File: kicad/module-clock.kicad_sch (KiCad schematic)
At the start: 9 parts, among them U1 NE555P

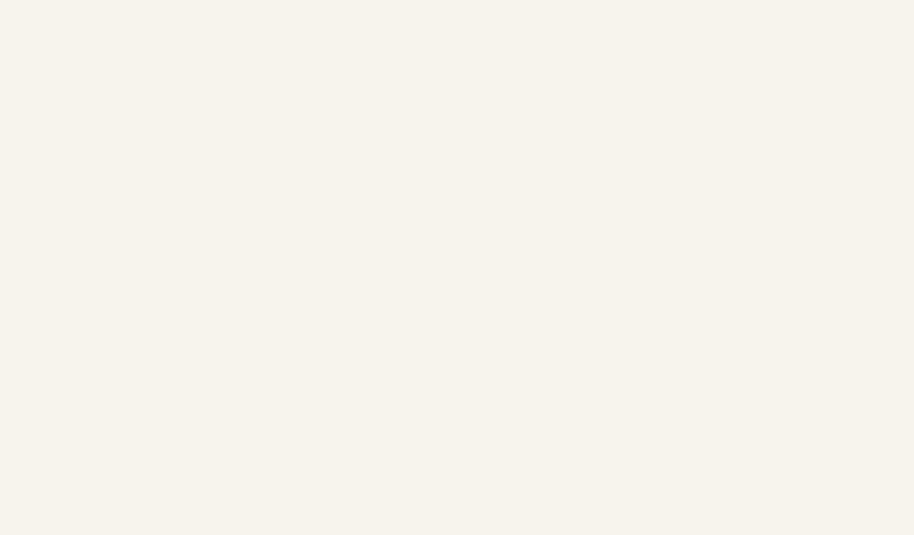
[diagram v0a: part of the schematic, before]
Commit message: Initial monostable mode implementation
Implement a monostable mode using the ne555 chip as a debouncer for the switch
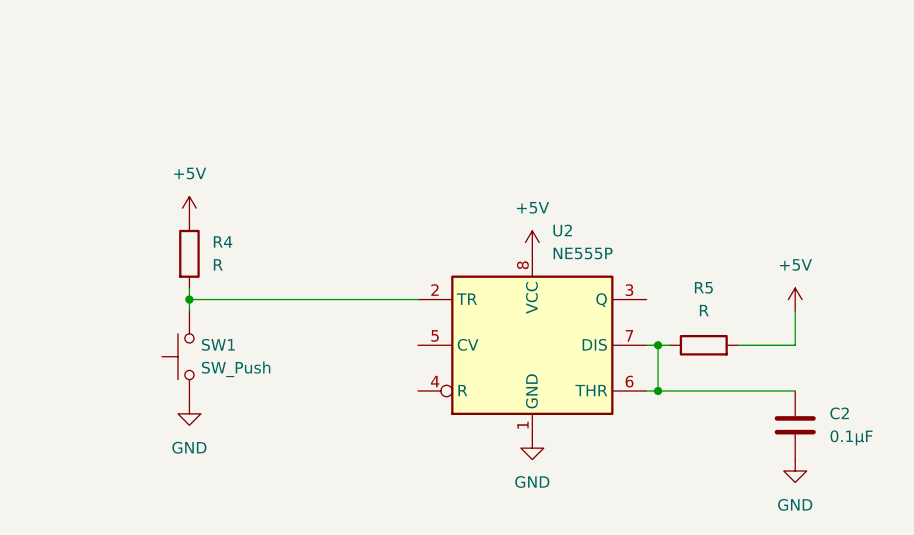
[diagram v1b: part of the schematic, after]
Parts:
- added C2: 0.1μF, symbol Device:C
- added R4, R5: R, symbol Device:R
- added SW1: SW_Push, symbol Switch:SW_Push
- added U2: NE555P, Package_DIP:DIP-8_W7.62mm, symbol Timer:NE555P
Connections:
- net +5V: now also R4.1, R5.2, U2.8 (VCC)
- net GND: now also C2.2, SW1.1, U2.1 (GND)
- new net: R4.2, SW1.2, U2.2 (TR)
- new net: C2.1, R5.1, U2.6 (THR), U2.7 (DIS)

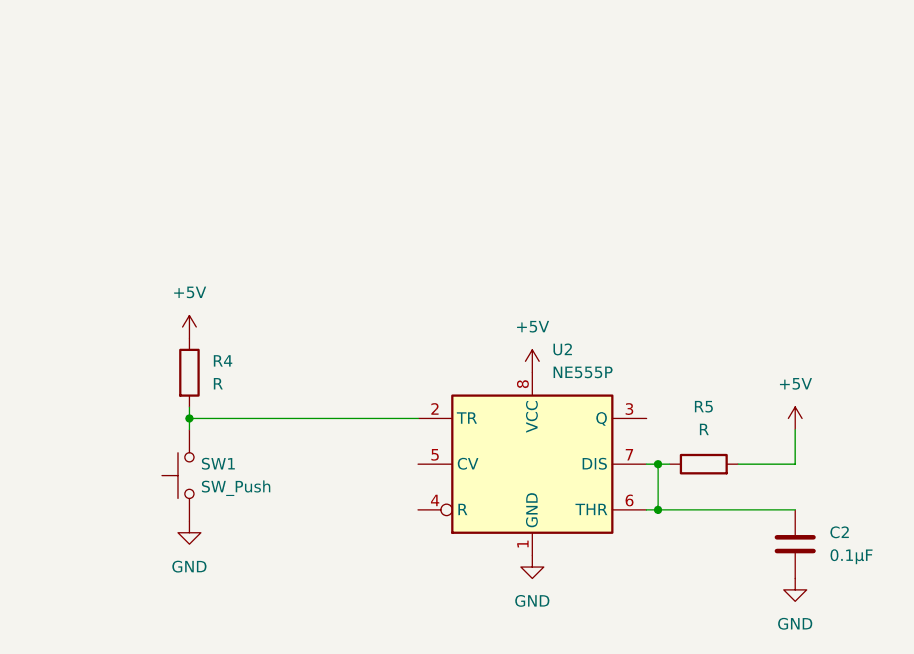
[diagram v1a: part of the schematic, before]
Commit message: Add LED status display
Use a LED to display when the button was pushed during monostable mode
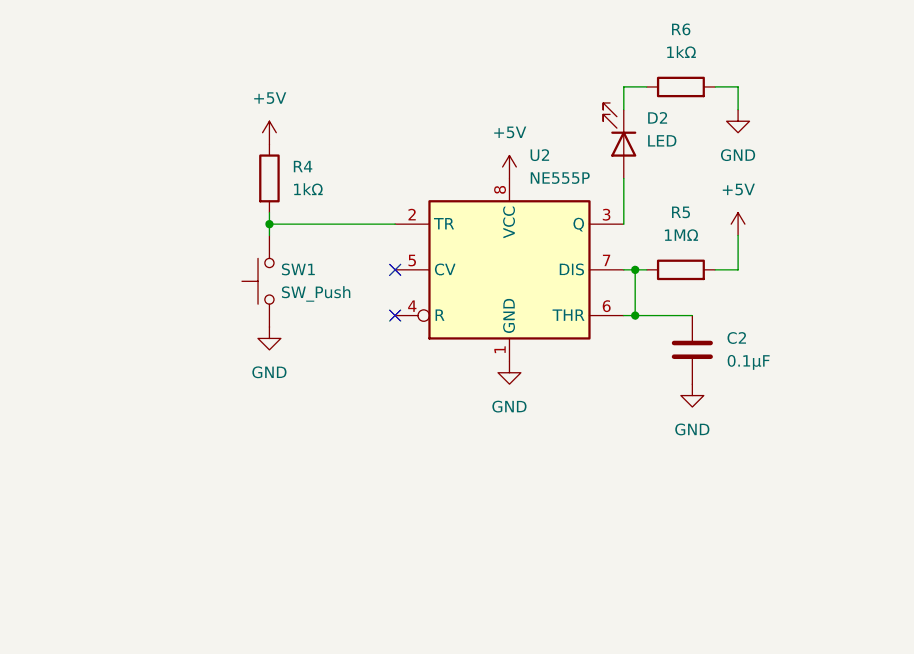
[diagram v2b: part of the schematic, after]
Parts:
- added D2: LED, symbol Device:LED
- added R6: 1kΩ, symbol Device:R
- R4: value R -> 1kΩ
- R5: value R -> 1MΩ
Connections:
- net GND: now also R6.2
- net at U2.3 (Q): now also D2.2 (A)
- new net: D2.1 (K), R6.1
- no-connect marks 0 -> 2
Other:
- moved on the sheet: C2, R4, R5, SW1, U2

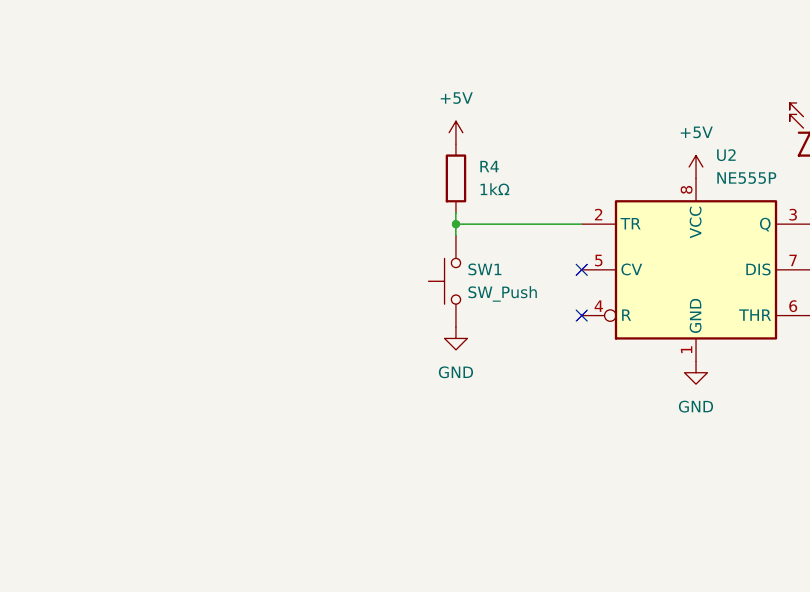
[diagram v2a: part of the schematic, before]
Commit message: Set pin 4 to HIGH and add a capacitor to pin 5
Set pin 4 to HIGH and add a capacitor to pin 5 for the NE555 timer
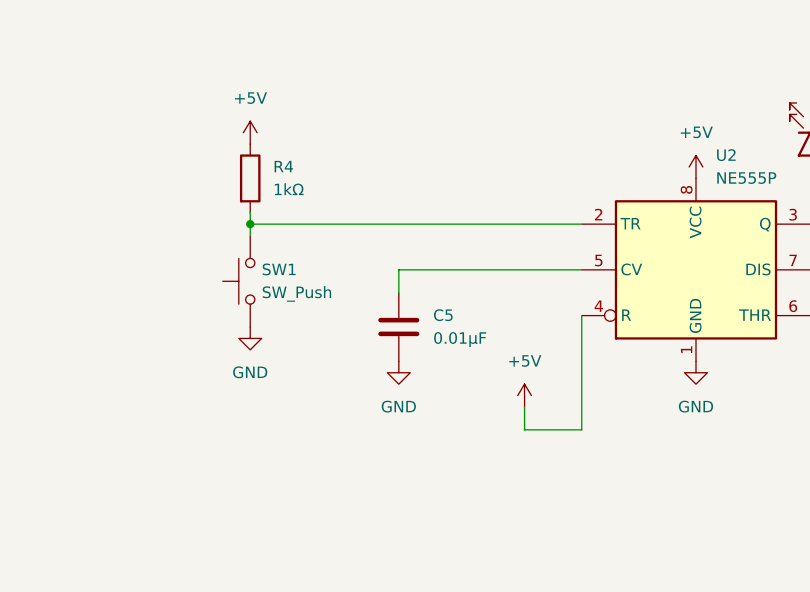
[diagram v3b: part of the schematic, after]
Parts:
- added C5: 0.01μF, symbol Device:C
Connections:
- net +5V: now also U2.4 (R)
- net GND: now also C5.2
- net at U2.5 (CV): now also C5.1
- no-connect marks 2 -> 0
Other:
- moved on the sheet: R4, SW1

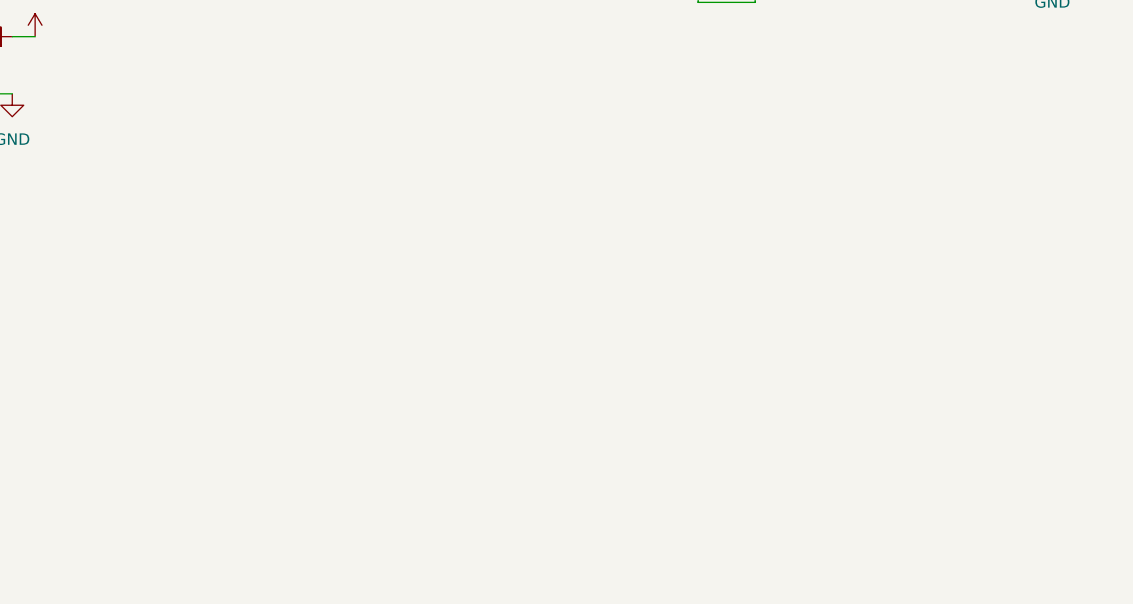
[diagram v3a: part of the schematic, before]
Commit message: Add bistable mode of the ne555
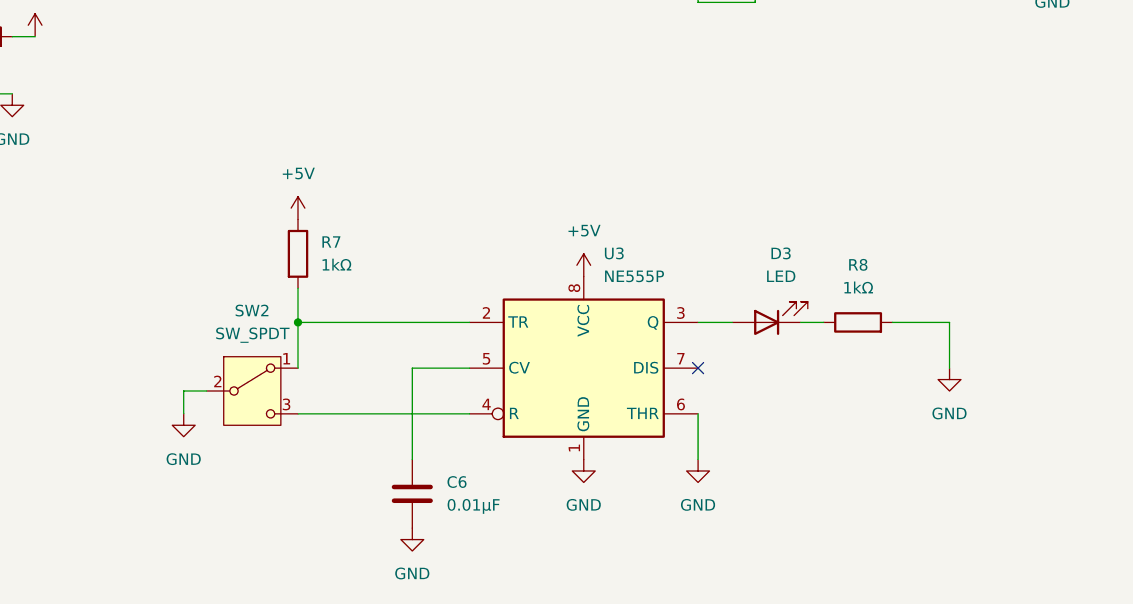
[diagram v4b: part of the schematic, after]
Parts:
- added C6: 0.01μF, symbol Device:C
- added D3: LED, symbol Device:LED
- added R7, R8: 1kΩ, symbol Device:R
- added SW2: SW_SPDT, symbol Switch:SW_SPDT
- added U3: NE555P, Package_DIP:DIP-8_W7.62mm, symbol Timer:NE555P
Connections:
- net +5V: now also R7.1, U3.8 (VCC)
- net GND: now also C6.2, R8.2, SW2.2 (B), U3.1 (GND), U3.6 (THR)
- new net: R7.2, SW2.1 (A), U3.2 (TR)
- new net: SW2.3 (C), U3.4 (R)
- new net: D3.1 (K), R8.1
- new net: D3.2 (A), U3.3 (Q)
- new net: C6.1, U3.5 (CV)
- no-connect marks 0 -> 1

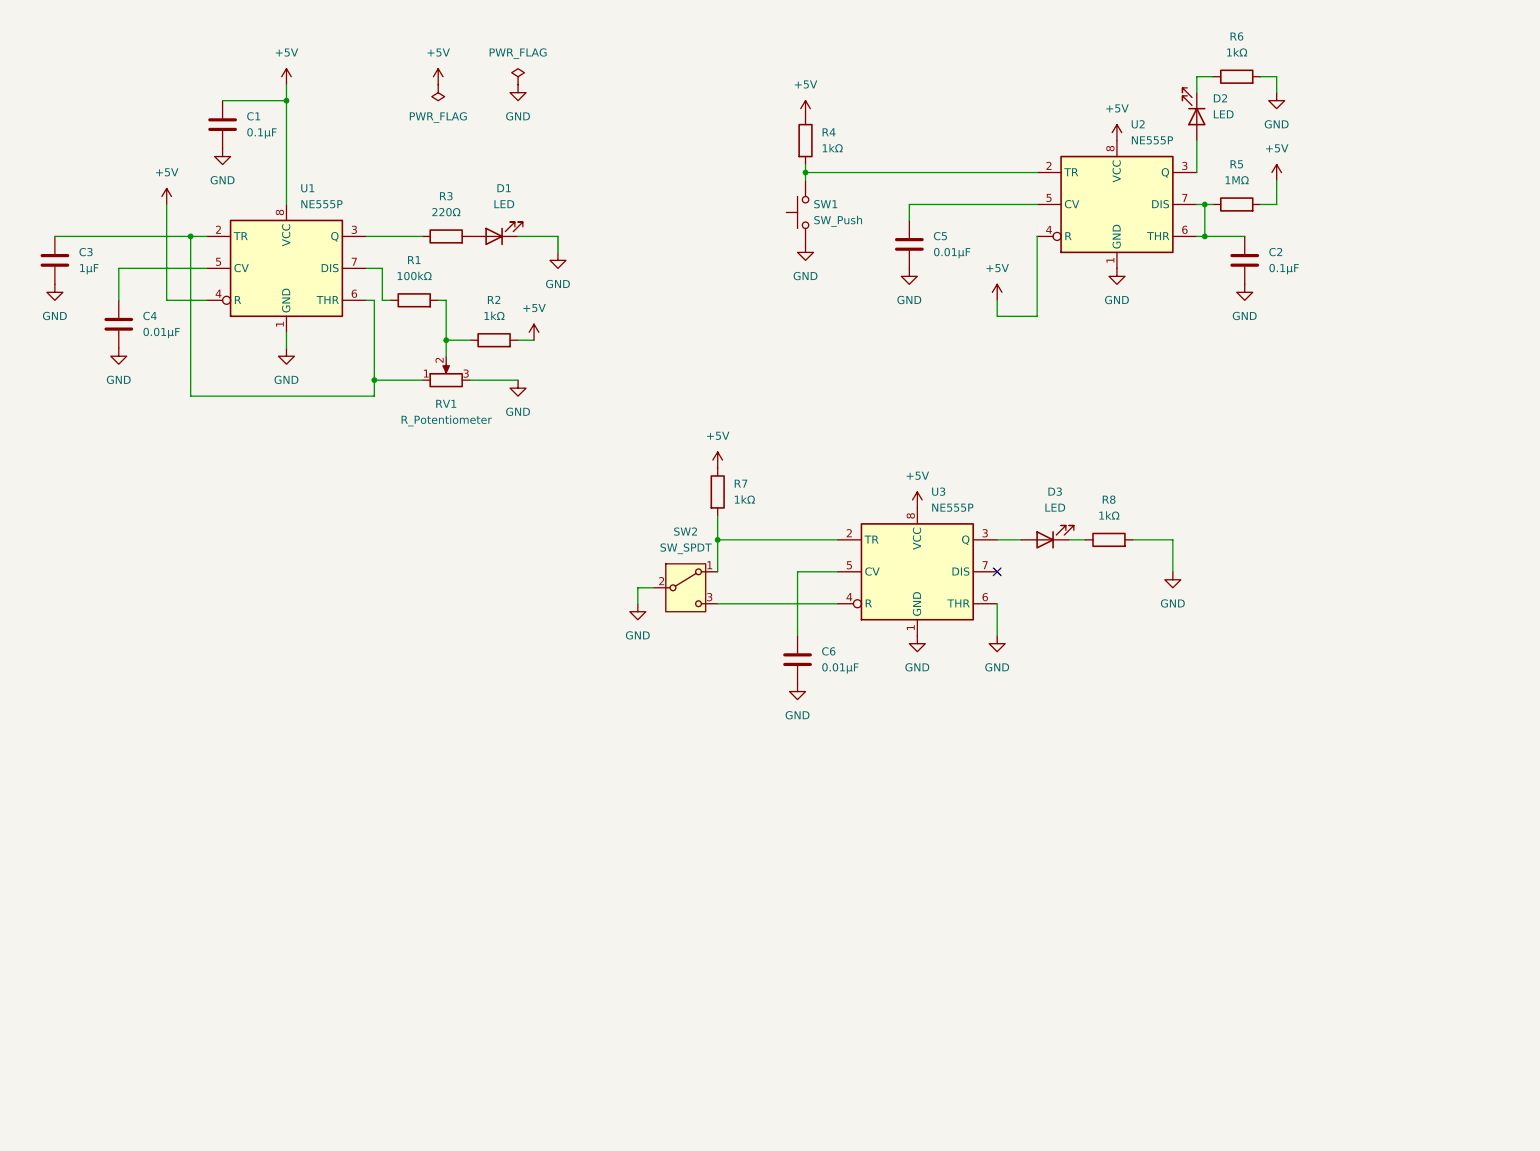
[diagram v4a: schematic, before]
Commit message: Add labels
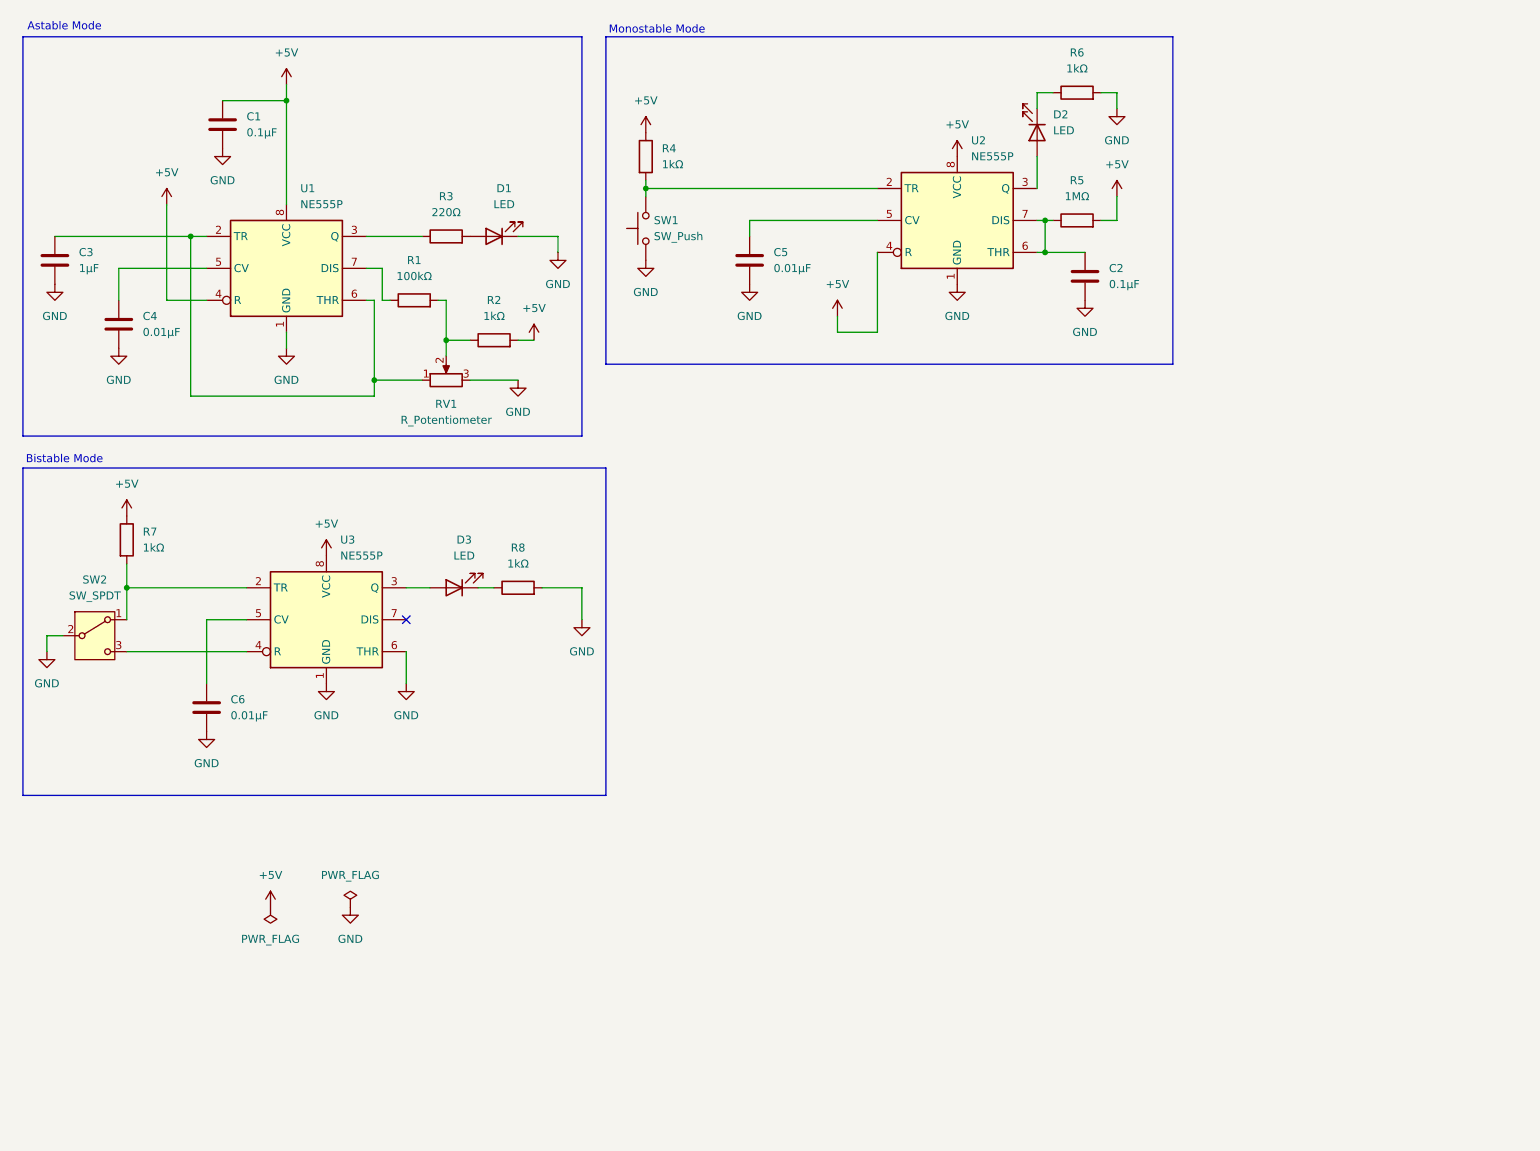
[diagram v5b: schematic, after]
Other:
- note added: "Astable Mode"
- note added: "Bistable Mode"
- note added: "Monostable Mode"
- moved on the sheet: C2, C5, C6, D2, D3, R4, R5, R6, R7, R8, SW1, SW2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
